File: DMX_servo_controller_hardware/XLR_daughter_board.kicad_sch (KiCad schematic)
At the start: 4 parts, among them J2 Conn_01x03_Pin, J3 XLR3

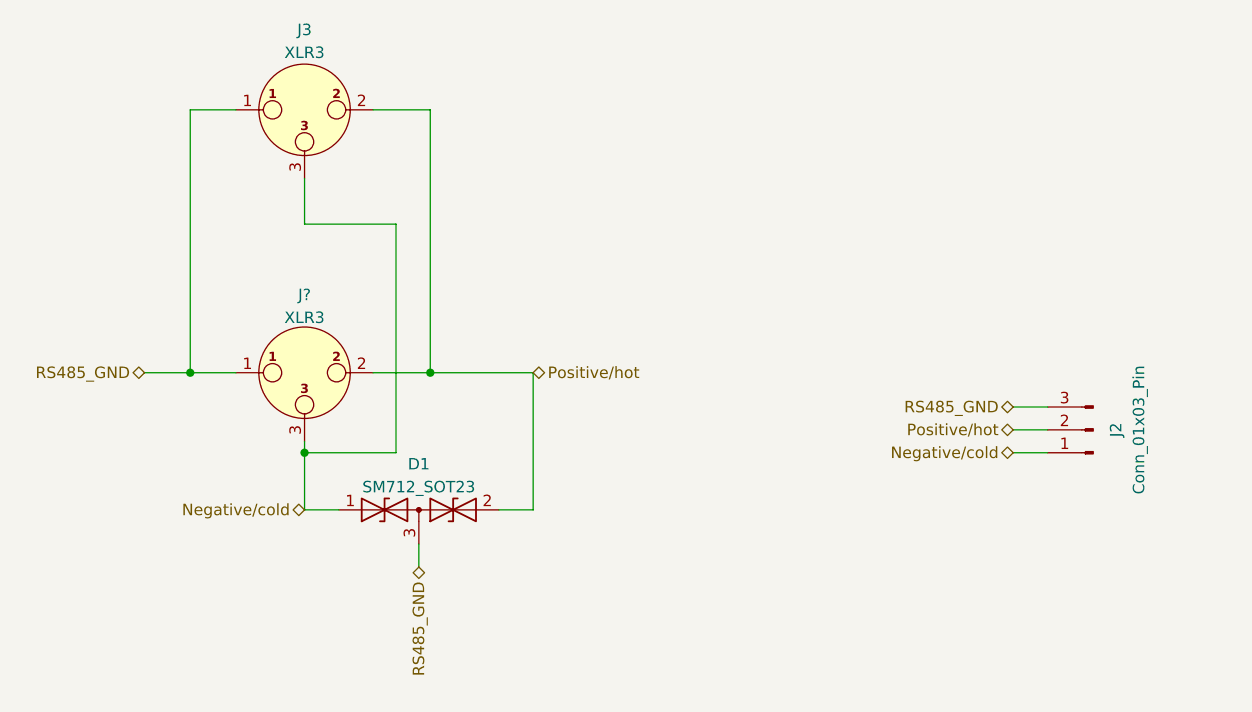
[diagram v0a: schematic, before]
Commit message: Adds Pi Pico to the schematics
This also adds a connector for 5V power (a screw terminal that will be
connected to the external power supply). The 3v3 rail will come from the
pico's regulator.
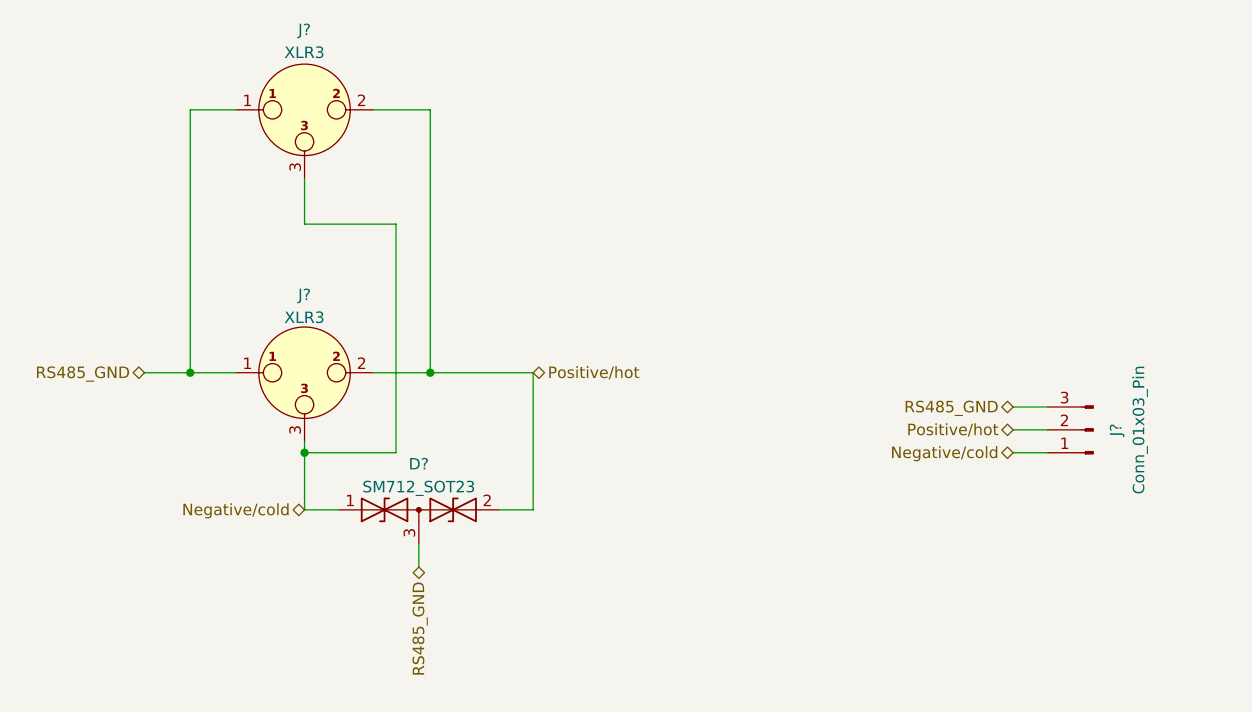
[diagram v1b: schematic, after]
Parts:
- renumbered D1 to D?, J3 to J?, J2 to J?
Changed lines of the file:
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@@
   (symbol (lib_id "Connector_Audio:XLR3") (at 118.11 64.77 0) (unit 1)
     (in_bom yes) (on_board yes) (dnp no) (fields_autoplaced)
-    (property "Reference" "J3" (at 118.11 55.88 0)
+    (property "Reference" "J?" (at 118.11 55.88 0)
       (effects (font (size 1.27 1.27)))
     )
@@
       (project "DMX_servo_controller_hardware"
         (path "/cd90393c-7fb4-4867-84b8-7df1a2bf6613/0cee26af-036e-49cb-9cbc-72ff24614e19"
-          (reference "J3") (unit 1)
+          (reference "J?") (unit 1)
         )
       )
@@
   (symbol (lib_id "Diode:SM712_SOT23") (at 130.81 109.22 0) (unit 1)
     (in_bom yes) (on_board yes) (dnp no) (fields_autoplaced)
-    (property "Reference" "D1" (at 130.81 104.14 0)
+    (property "Reference" "D?" (at 130.81 104.14 0)
       (effects (font (size 1.27 1.27)))
     )
@@
       (project "DMX_servo_controller_hardware"
         (path "/cd90393c-7fb4-4867-84b8-7df1a2bf6613"
-          (reference "D1") (unit 1)
+          (reference "D?") (unit 1)
         )
         (path "/cd90393c-7fb4-4867-84b8-7df1a2bf6613/0cee26af-036e-49cb-9cbc-72ff24614e19"
-          (reference "D1") (unit 1)
+          (reference "D?") (unit 1)
         )
       )
@@
   (symbol (lib_id "Connector:Conn_01x03_Pin") (at 205.74 100.33 180) (unit 1)
     (in_bom yes) (on_board yes) (dnp no) (fields_autoplaced)
-    (property "Reference" "J2" (at 208.28 100.33 90)
+    (property "Reference" "J?" (at 208.28 100.33 90)
       (effects (font (size 1.27 1.27)))
     )
@@
       (project "DMX_servo_controller_hardware"
         (path "/cd90393c-7fb4-4867-84b8-7df1a2bf6613/0cee26af-036e-49cb-9cbc-72ff24614e19"
-          (reference "J2") (unit 1)
+          (reference "J?") (unit 1)
         )
       )
@@
         )
         (path "/cd90393c-7fb4-4867-84b8-7df1a2bf6613/0cee26af-036e-49cb-9cbc-72ff24614e19"
-          (reference "J1") (unit 1)
+          (reference "J?") (unit 1)
         )
       )

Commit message: FIxes ERC errors
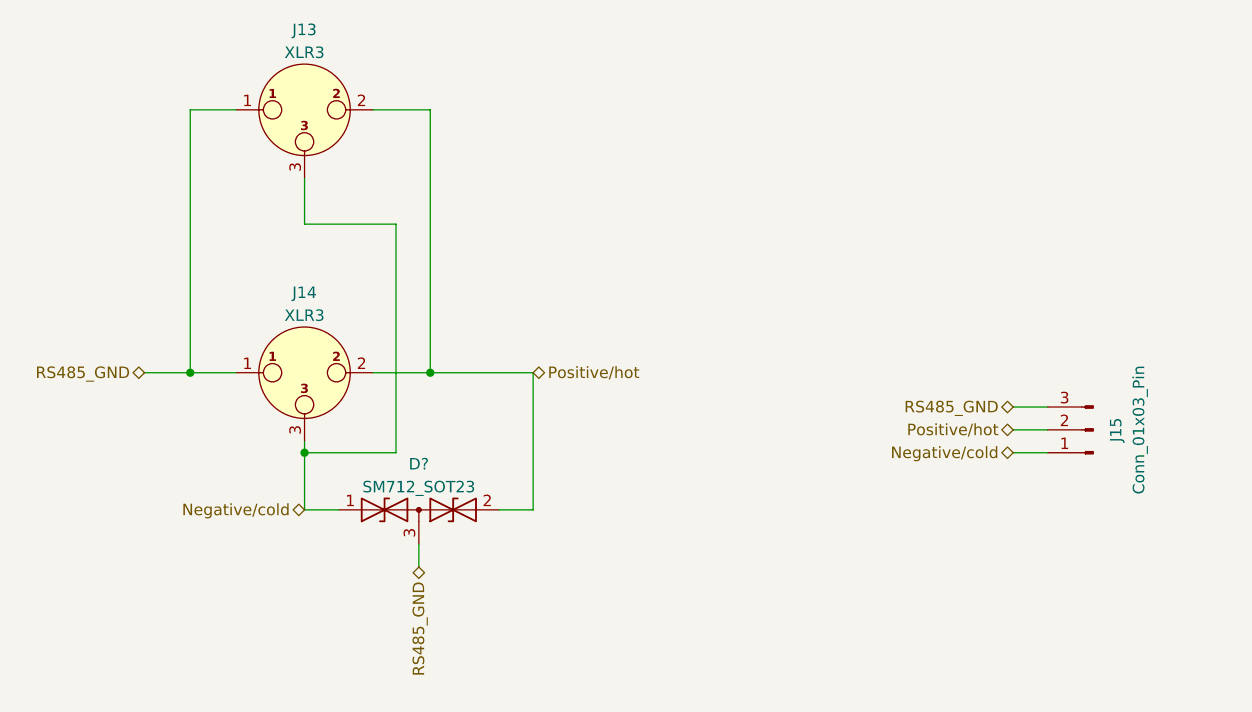
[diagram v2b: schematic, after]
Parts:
- removed J?: XLR3, symbol Connector:XLR3
- added J14: XLR3, symbol Connector_Audio:XLR3
- gave numbers to parts that had none: 2
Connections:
- net Negative/cold: now also J14.3
- net Positive/hot: now also J14.2
- net RS485_GND: now also J14.1
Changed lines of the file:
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@@
   (symbol (lib_id "Connector_Audio:XLR3") (at 118.11 64.77 0) (unit 1)
     (in_bom yes) (on_board yes) (dnp no) (fields_autoplaced)
-    (property "Reference" "J?" (at 118.11 55.88 0)
+    (property "Reference" "J13" (at 118.11 55.88 0)
       (effects (font (size 1.27 1.27)))
     )
@@
       (project "DMX_servo_controller_hardware"
         (path "/cd90393c-7fb4-4867-84b8-7df1a2bf6613/0cee26af-036e-49cb-9cbc-72ff24614e19"
-          (reference "J?") (unit 1)
+          (reference "J13") (unit 1)
+        )
+      )
+    )
+  )
+  (symbol (lib_id "Connector_Audio:XLR3") (at 118.11 93.98 0) (unit 1)
+    (in_bom yes) (on_board yes) (dnp no) (fields_autoplaced)
+    (property "Reference" "J14" (at 118.11 85.09 0)
+      (effects (font (size 1.27 1.27)))
+    )
+    (property "Value" "XLR3" (at 118.11 87.63 0)
+      (effects (font (size 1.27 1.27)))
+    )
+    (property "Footprint" "" (at 118.11 93.98 0)
+      (effects (font (size 1.27 1.27)) hide)
+    )
+    (property "Datasheet" " ~" (at 118.11 93.98 0)
+      (effects (font (size 1.27 1.27)) hide)
+    )
+    (pin "1")
+    (pin "2")
+    (pin "3")
+    (instances
+      (project "DMX_servo_controller_hardware"
+        (path "/cd90393c-7fb4-4867-84b8-7df1a2bf6613/0cee26af-036e-49cb-9cbc-72ff24614e19"
+          (reference "J14") (unit 1)
         )
       )
@@
         )
         (path "/cd90393c-7fb4-4867-84b8-7df1a2bf6613/0cee26af-036e-49cb-9cbc-72ff24614e19"
-          (reference "D?") (unit 1)
+          (reference "D1") (unit 1)
         )
       )
@@
   (symbol (lib_id "Connector:Conn_01x03_Pin") (at 205.74 100.33 180) (unit 1)
     (in_bom yes) (on_board yes) (dnp no) (fields_autoplaced)
-    (property "Reference" "J?" (at 208.28 100.33 90)
+    (property "Reference" "J15" (at 208.28 100.33 90)
       (effects (font (size 1.27 1.27)))
     )
@@
       (project "DMX_servo_controller_hardware"
         (path "/cd90393c-7fb4-4867-84b8-7df1a2bf6613/0cee26af-036e-49cb-9cbc-72ff24614e19"
-          (reference "J?") (unit 1)
+          (reference "J15") (unit 1)
         )
       )
-    )
-  )
-  (symbol (lib_id "Connector:XLR3") (at 118.11 93.98 0) (unit 1)
-    (in_bom yes) (on_board yes) (dnp no) (fields_autoplaced)
-    (property "Reference" "J?" (at 118.11 85.3272 0)
-      (effects (font (size 1.27 1.27)))
-    )
-    (property "Value" "XLR3" (at 118.11 87.8641 0)
-      (effects (font (size 1.27 1.27)))
-    )
-    (property "Footprint" "" (at 118.11 93.98 0)
-      (effects (font (size 1.27 1.27)) hide)
-    )
-    (property "Datasheet" " ~" (at 118.11 93.98 0)
-      (effects (font (size 1.27 1.27)) hide)
-    )
-    (pin "1")
-    (pin "2")
-    (pin "3")
-    (instances
-      (project "DMX_servo_controller_hardware"
-        (path "/cd90393c-7fb4-4867-84b8-7df1a2bf6613"
-          (reference "J?") (unit 1)
-        )
-        (path "/cd90393c-7fb4-4867-84b8-7df1a2bf6613/0cee26af-036e-49cb-9cbc-72ff24614e19"
-          (reference "J?") (unit 1)
-        )
-      )

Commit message: Fixes schematics symbols that were triggering ERC errors
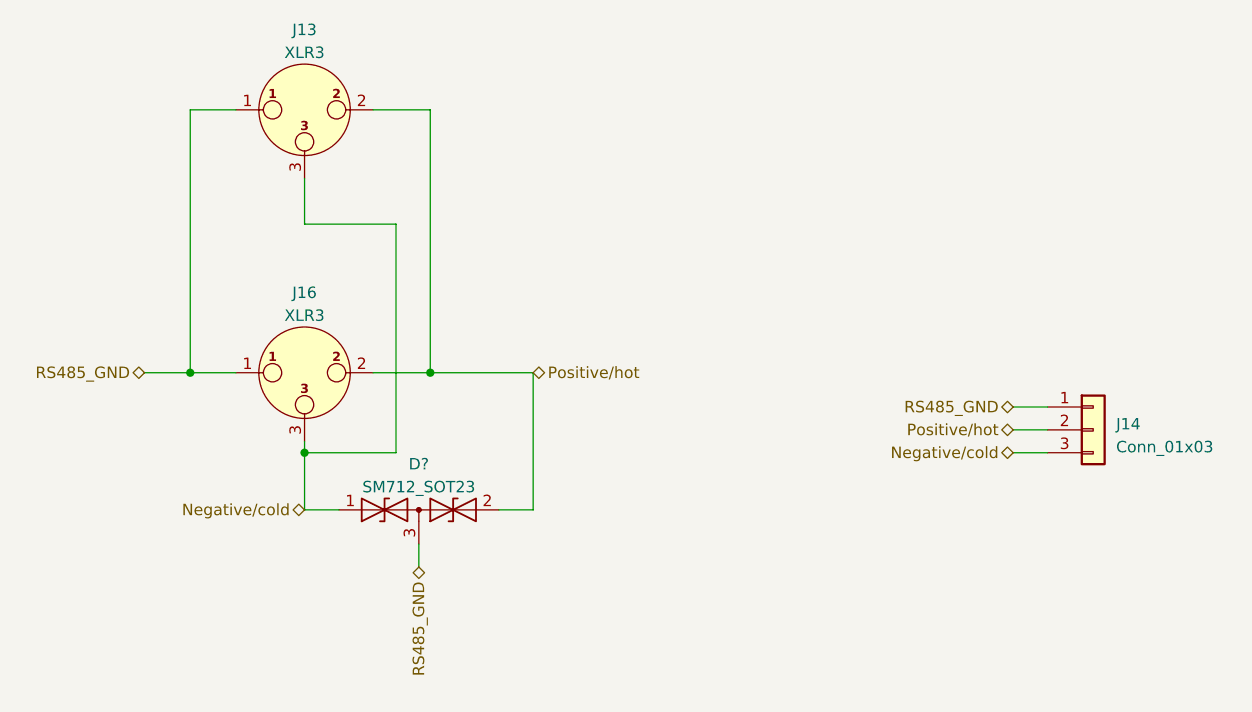
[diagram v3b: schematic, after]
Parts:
- removed J13, J14: XLR3, symbol Connector_Audio:XLR3
- removed J15: Conn_01x03_Pin, symbol Connector:Conn_01x03_Pin
- added J13, J16: XLR3, symbol Connector:XLR3
- added J14: Conn_01x03, symbol Connector_Generic:Conn_01x03
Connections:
- net Negative/cold: now also J13.3, J14.3 (Pin_3), J16.3
- net Positive/hot: now also J13.2, J14.2 (Pin_2), J16.2
- net RS485_GND: now also J13.1, J14.1 (Pin_1), J16.1
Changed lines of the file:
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@@
     (effects (font (size 1.27 1.27)) (justify right))
   )
-  (symbol (lib_id "Connector_Audio:XLR3") (at 118.11 64.77 0) (unit 1)
+  (symbol (lib_id "Connector_Generic:Conn_01x03") (at 205.74 100.33 0) (unit 1)
+    (in_bom yes) (on_board yes) (dnp no) (fields_autoplaced)
+    (property "Reference" "J14" (at 208.28 99.695 0)
+      (effects (font (size 1.27 1.27)) (justify left))
+    )
+    (property "Value" "Conn_01x03" (at 208.28 102.235 0)
+      (effects (font (size 1.27 1.27)) (justify left))
+    )
+    (property "Footprint" "" (at 205.74 100.33 0)
+      (effects (font (size 1.27 1.27)) hide)
+    )
+    (property "Datasheet" "~" (at 205.74 100.33 0)
+      (effects (font (size 1.27 1.27)) hide)
+    )
+    (pin "1")
+    (pin "2")
+    (pin "3")
+    (instances
+      (project "DMX_servo_controller_hardware"
+        (path "/cd90393c-7fb4-4867-84b8-7df1a2bf6613/0cee26af-036e-49cb-9cbc-72ff24614e19"
+          (reference "J14") (unit 1)
+        )
+      )
+    )
+  )
+  (symbol (lib_id "Connector:XLR3") (at 118.11 64.77 0) (unit 1)
     (in_bom yes) (on_board yes) (dnp no) (fields_autoplaced)
     (property "Reference" "J13" (at 118.11 55.88 0)
@@
         (path "/cd90393c-7fb4-4867-84b8-7df1a2bf6613/0cee26af-036e-49cb-9cbc-72ff24614e19"
           (reference "J13") (unit 1)
-        )
-      )
-    )
-  )
-  (symbol (lib_id "Connector_Audio:XLR3") (at 118.11 93.98 0) (unit 1)
-    (in_bom yes) (on_board yes) (dnp no) (fields_autoplaced)
-    (property "Reference" "J14" (at 118.11 85.09 0)
-      (effects (font (size 1.27 1.27)))
-    )
-    (property "Value" "XLR3" (at 118.11 87.63 0)
-      (effects (font (size 1.27 1.27)))
-    )
-    (property "Footprint" "" (at 118.11 93.98 0)
-      (effects (font (size 1.27 1.27)) hide)
-    )
-    (property "Datasheet" " ~" (at 118.11 93.98 0)
-      (effects (font (size 1.27 1.27)) hide)
-    )
-    (pin "1")
-    (pin "2")
-    (pin "3")
-    (instances
-      (project "DMX_servo_controller_hardware"
-        (path "/cd90393c-7fb4-4867-84b8-7df1a2bf6613/0cee26af-036e-49cb-9cbc-72ff24614e19"
-          (reference "J14") (unit 1)
         )
       )
@@
     )
   )
-  (symbol (lib_id "Connector:Conn_01x03_Pin") (at 205.74 100.33 180) (unit 1)
+  (symbol (lib_id "Connector:XLR3") (at 118.11 93.98 0) (unit 1)
     (in_bom yes) (on_board yes) (dnp no) (fields_autoplaced)
-    (property "Reference" "J15" (at 208.28 100.33 90)
+    (property "Reference" "J16" (at 118.11 85.09 0)
       (effects (font (size 1.27 1.27)))
     )
-    (property "Value" "Conn_01x03_Pin" (at 210.82 100.33 90)
+    (property "Value" "XLR3" (at 118.11 87.63 0)
       (effects (font (size 1.27 1.27)))
     )
-    (property "Footprint" "" (at 205.74 100.33 0)
+    (property "Footprint" "" (at 118.11 93.98 0)
       (effects (font (size 1.27 1.27)) hide)
     )
-    (property "Datasheet" "~" (at 205.74 100.33 0)
+    (property "Datasheet" " ~" (at 118.11 93.98 0)
       (effects (font (size 1.27 1.27)) hide)
     )
@@
       (project "DMX_servo_controller_hardware"
         (path "/cd90393c-7fb4-4867-84b8-7df1a2bf6613/0cee26af-036e-49cb-9cbc-72ff24614e19"
-          (reference "J15") (unit 1)
+          (reference "J16") (unit 1)
         )
       )

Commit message: Reasigns component designators
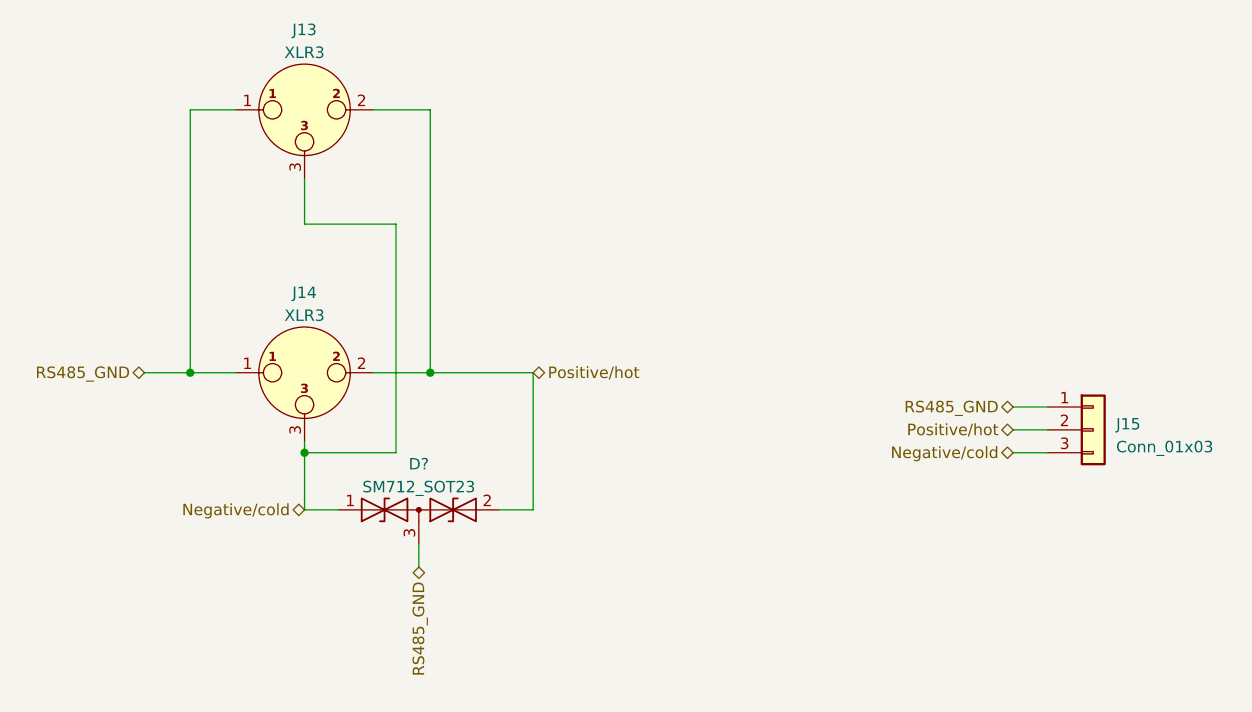
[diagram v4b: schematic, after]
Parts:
- renumbered J16 to J14, J14 to J15
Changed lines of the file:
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@@
   (symbol (lib_id "Connector_Generic:Conn_01x03") (at 205.74 100.33 0) (unit 1)
     (in_bom yes) (on_board yes) (dnp no) (fields_autoplaced)
-    (property "Reference" "J14" (at 208.28 99.695 0)
+    (property "Reference" "J15" (at 208.28 99.695 0)
       (effects (font (size 1.27 1.27)) (justify left))
     )
@@
       (project "DMX_servo_controller_hardware"
         (path "/cd90393c-7fb4-4867-84b8-7df1a2bf6613/0cee26af-036e-49cb-9cbc-72ff24614e19"
-          (reference "J14") (unit 1)
+          (reference "J15") (unit 1)
         )
       )
@@
         )
         (path "/cd90393c-7fb4-4867-84b8-7df1a2bf6613/0cee26af-036e-49cb-9cbc-72ff24614e19"
-          (reference "D1") (unit 1)
+          (reference "D2") (unit 1)
         )
       )
@@
   (symbol (lib_id "Connector:XLR3") (at 118.11 93.98 0) (unit 1)
     (in_bom yes) (on_board yes) (dnp no) (fields_autoplaced)
-    (property "Reference" "J16" (at 118.11 85.09 0)
+    (property "Reference" "J14" (at 118.11 85.09 0)
       (effects (font (size 1.27 1.27)))
     )
@@
       (project "DMX_servo_controller_hardware"
         (path "/cd90393c-7fb4-4867-84b8-7df1a2bf6613/0cee26af-036e-49cb-9cbc-72ff24614e19"
-          (reference "J16") (unit 1)
+          (reference "J14") (unit 1)
         )
       )

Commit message: Assigns footprints to some of the components
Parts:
- J15: footprint (none) -> Connector_JST:JST_XH_B3B-XH-AM_1x03_P2.50mm_Vertical
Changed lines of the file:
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@@
       (effects (font (size 1.27 1.27)) (justify left))
     )
-    (property "Footprint" "" (at 205.74 100.33 0)
+    (property "Footprint" "Connector_JST:JST_XH_B3B-XH-AM_1x03_P2.50mm_Vertical" (at 205.74 100.33 0)
       (effects (font (size 1.27 1.27)) hide)
     )
